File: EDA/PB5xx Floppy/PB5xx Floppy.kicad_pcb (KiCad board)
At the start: 2 copper layers, 20 x 60 mm, 6 parts, among them J1 PowerBook, J2 IDC20

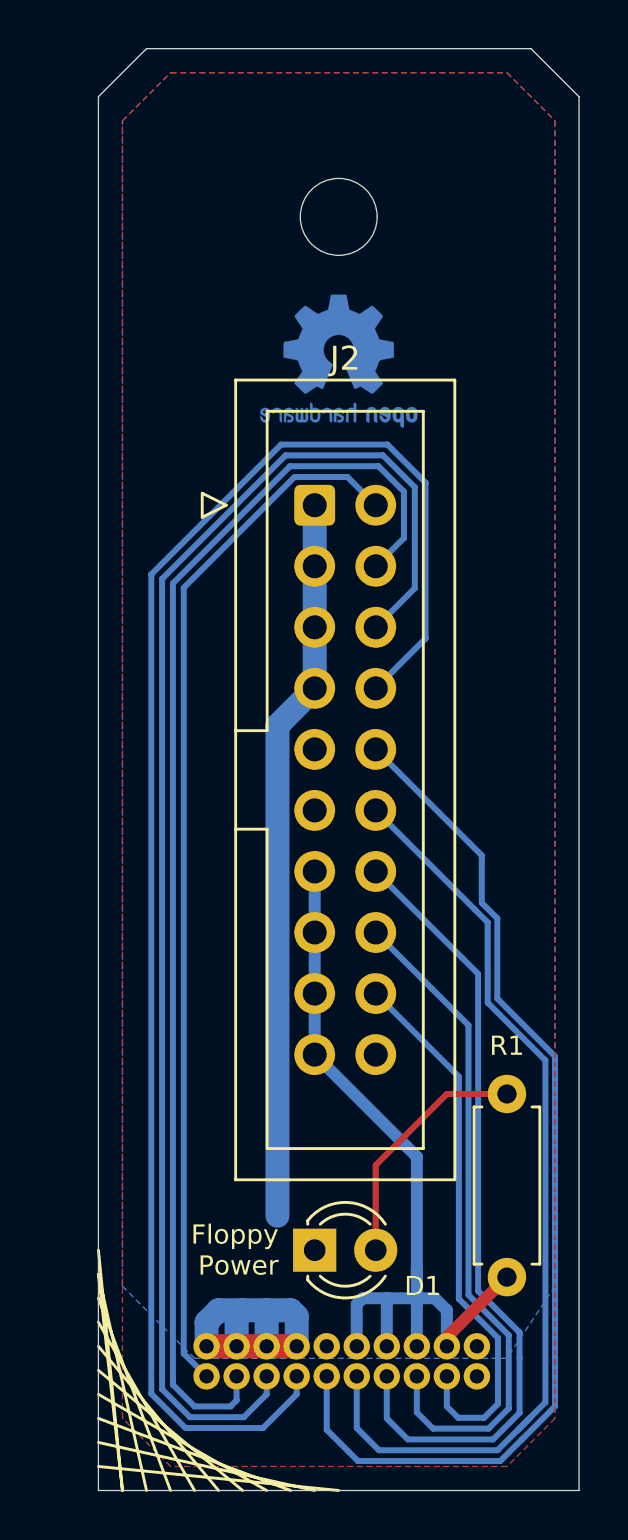
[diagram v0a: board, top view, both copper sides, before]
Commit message: PB5xx Floppy v1.2: respin adapter for use in BBRX77
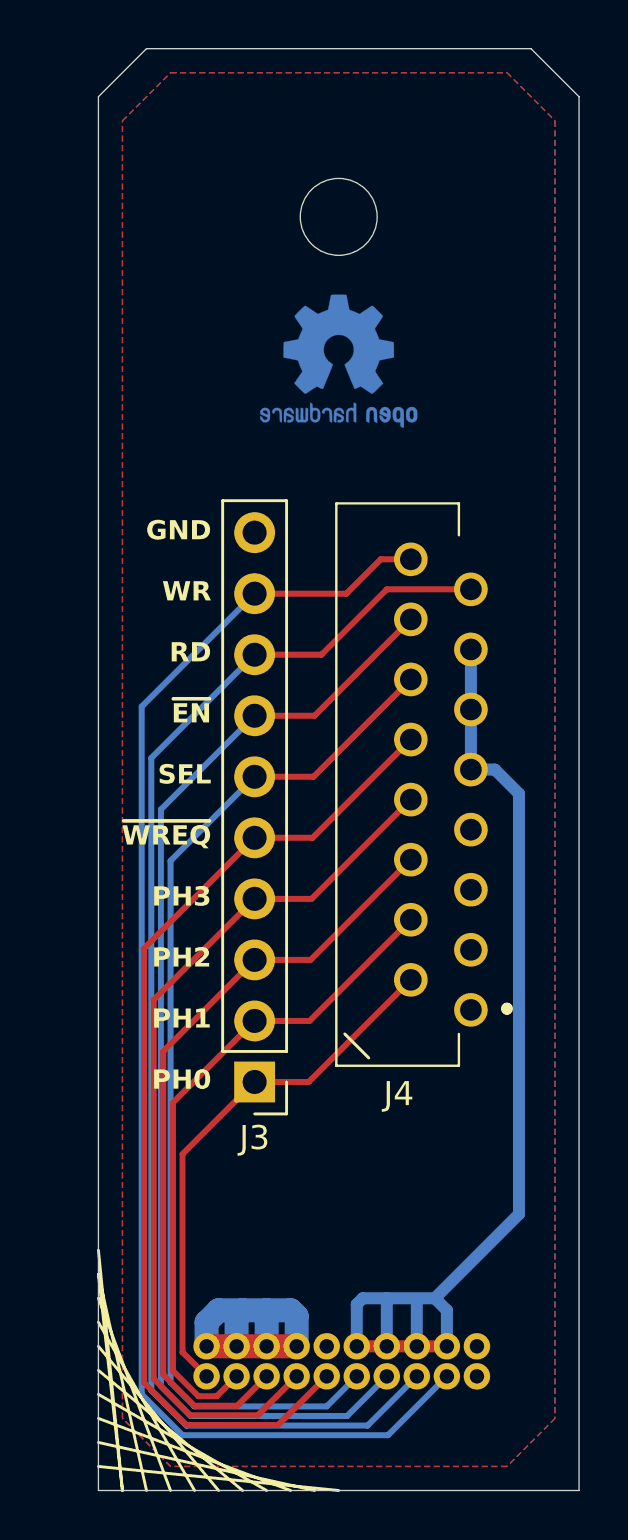
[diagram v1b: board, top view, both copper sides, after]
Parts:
- removed D1: LED, LED_THT:LED_D3.0mm
- removed J2: IDC20, Connector_IDC:IDC-Header_2x10_P2.54mm_Vertical
- removed R1: 300, Resistor_THT:R_Axial_DIN0207_L6.3mm_D2.5mm_P7.62mm_Horizontal
- added J3: Conn_01x10, Connector_PinHeader_2.54mm:PinHeader_1x10_P2.54mm_Vertical, F.Cu at (46.5, 153.0)
- added J4: 52045-1645, PB5xx Floppy:52045-1645, F.Cu at (55.5, 150.0)
- J1: footprint G125-MV12005L0P:G125-MV12005L0P -> PB5xx Floppy:G125-MV12005L0P
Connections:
- J1 pad 10: (no net) -> unconnected-(J1-Pin_10-Pad10)
- J1 pad 15: /~WREQ -> /~{WREQ}
- J1 pad 17: /~ENABLE -> /~{ENABLE}
- J1 pad 20: (no net) -> unconnected-(J1-Pin_20-Pad20)
- J1 pad 5: (no net) -> unconnected-(J1-Pin_5-Pad5)
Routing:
- net /~{ENABLE}: track 0.00 -> 48.3 mm
- net /~WREQ: track 43.6 -> 0.00 mm
- net /~{WREQ}: track 0.00 -> 41.9 mm
- net /WR: track 23.0 -> 56.8 mm
- net /~ENABLE: track 33.1 -> 0.00 mm
- net GND: track 43.4 -> 13.2 mm
- net /PH3: track 65.8 -> 37.2 mm
- net /PH2: track 59.4 -> 32.4 mm
- net /RD: track 28.1 -> 55.0 mm
- net /PH1: track 53.1 -> 27.6 mm
- net /PH0: track 43.6 -> 22.2 mm
- net Net-(D1-Pad2): track 10.2 -> 0.00 mm
- net +5V: track 35.4 -> 44.7 mm
- net /SEL: track 39.5 -> 43.5 mm
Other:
- net class +VCC removed
- net class Default removed
- net class GND removed
- board text added: "GND"
- board text added: "PH0"
- board text added: "PH1"
- board text added: "PH2"
- board text added: "PH3"
- board text added: "PowerBook 5xx Floppy interconnect board"
- board text added: "RD"
- board text added: "SEL"
- board text added: "WR"
- board text added: "~{EN}"
- board text added: "~{WREQ}"
- board text removed: "Floppy Power"
- board text removed: "PowerBook 5xx Floppy to Desktop Macintosh"
